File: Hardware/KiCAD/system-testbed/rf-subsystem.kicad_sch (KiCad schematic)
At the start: 86 parts, among them P1 SMA, P3 SMA, SW3 SKY13330-397LF, SW5 SKY13330-397LF, U3 CC1200RHBR, U4 TXS0101DBV, U6 LP5907MFX-2.5, X3 40 MHz

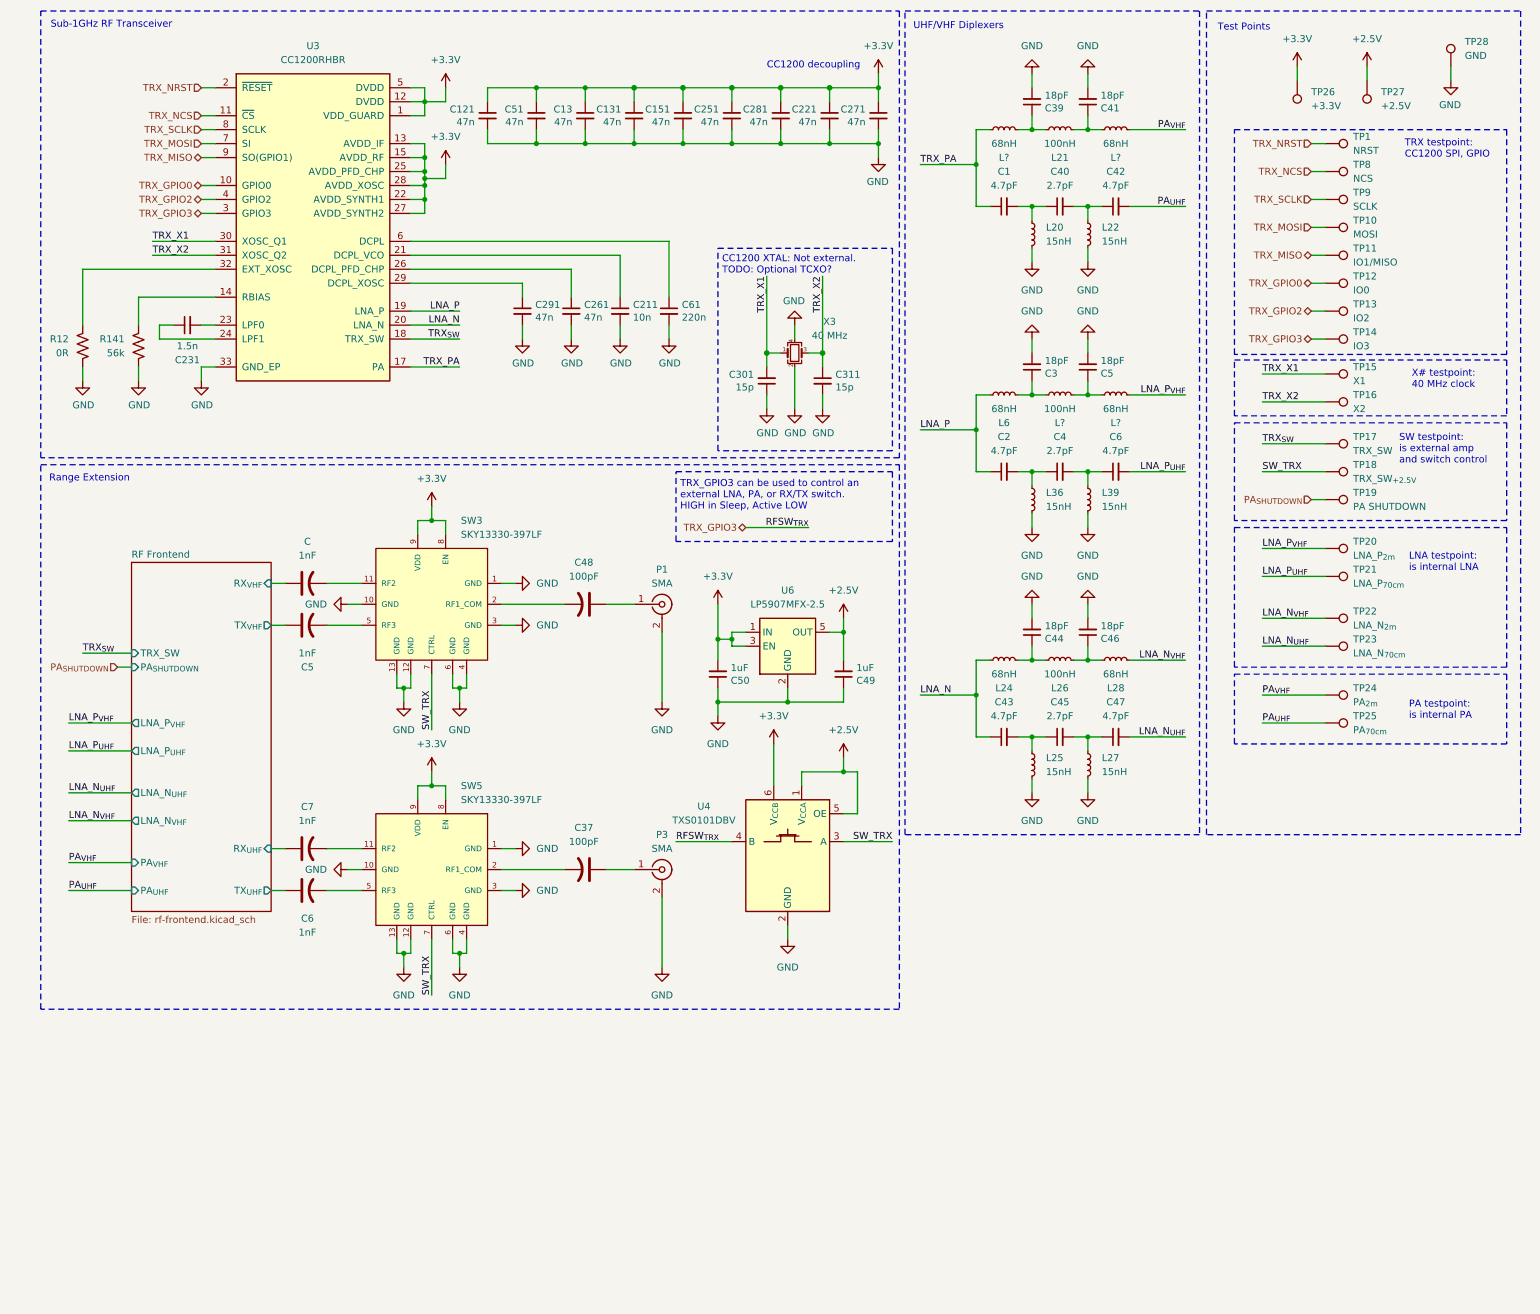
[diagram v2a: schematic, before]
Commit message: fix: reannotate schematics for pcb editor use #55
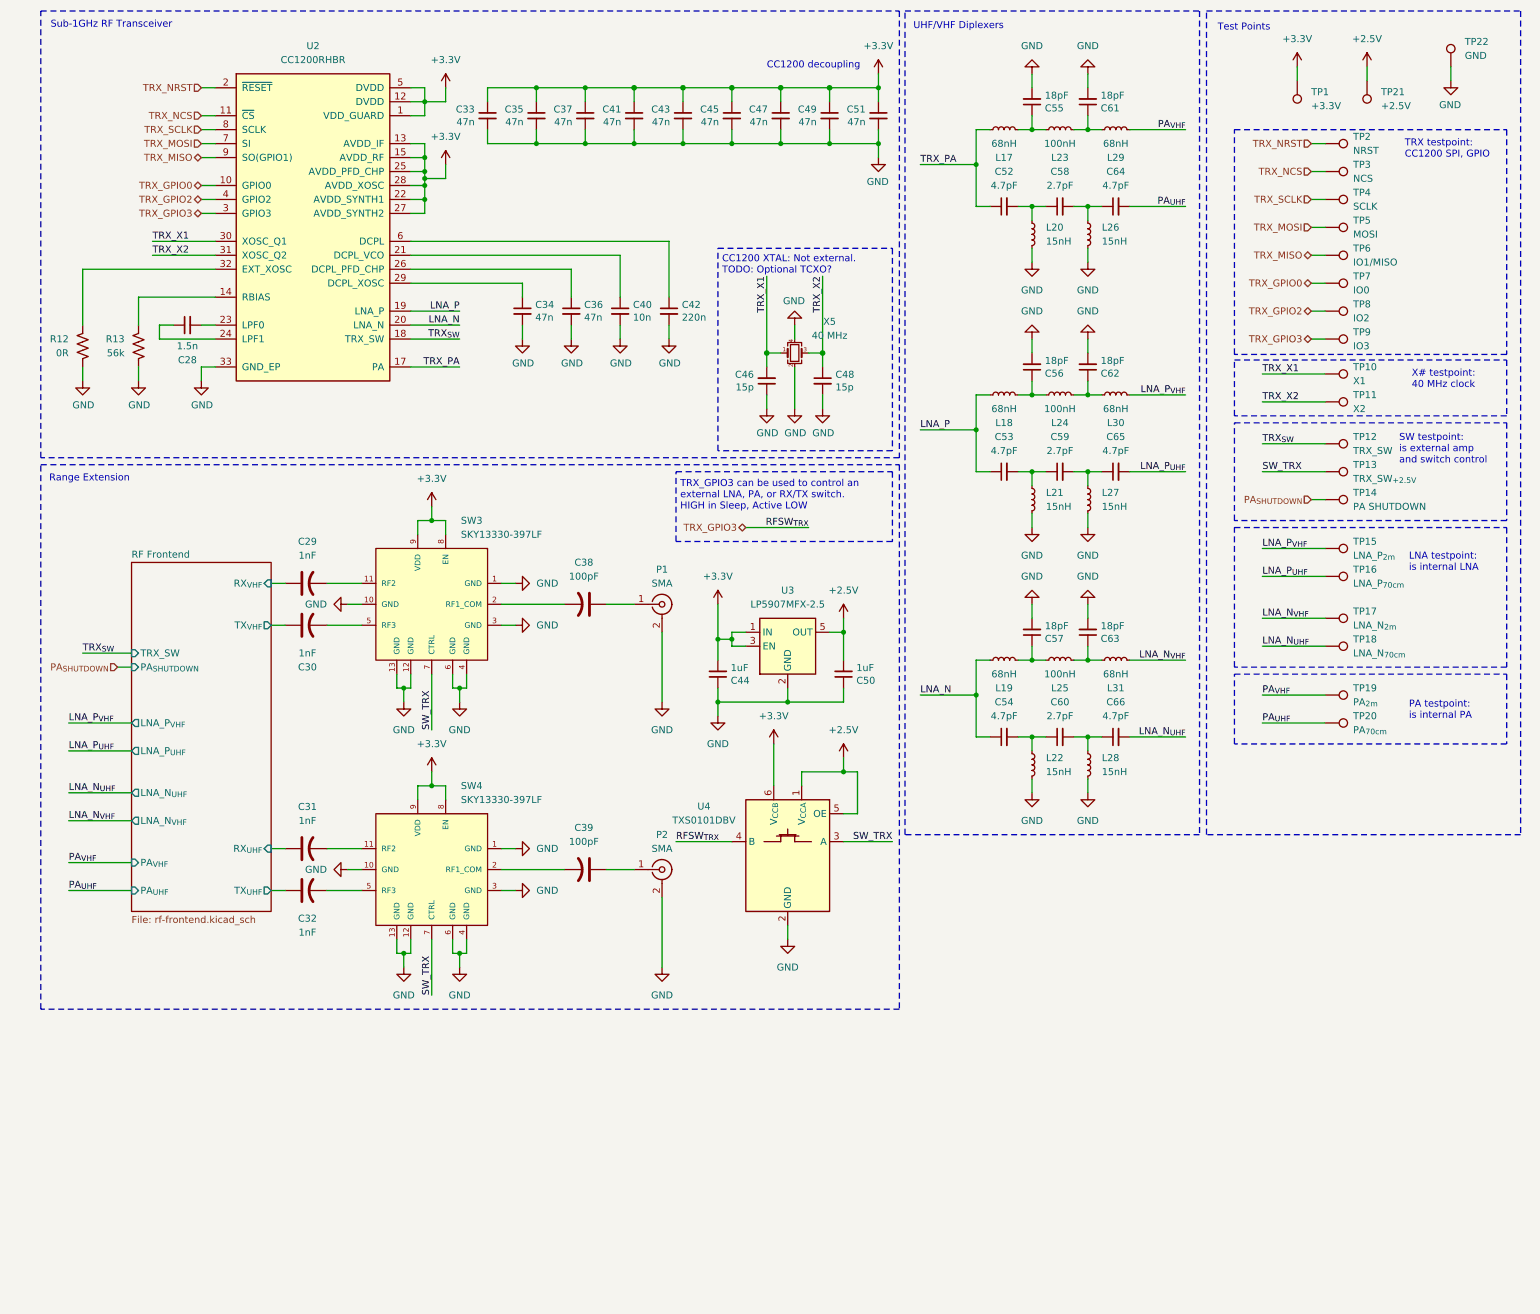
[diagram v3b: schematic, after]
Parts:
- C28: renamed from C231; footprint Capacitor_SMD:C_0603_1608Metric -> Capacitor_SMD:C_0402_1005Metric
- C29: renamed from C; footprint Capacitor_SMD:C_0603_1608Metric -> Capacitor_SMD:C_0402_1005Metric
- C30, C62: renamed from C5; footprint Capacitor_SMD:C_0603_1608Metric -> Capacitor_SMD:C_0402_1005Metric
- C31: renamed from C7; footprint Capacitor_SMD:C_0603_1608Metric -> Capacitor_SMD:C_0402_1005Metric
- C32: renamed from C6; footprint Capacitor_SMD:C_0603_1608Metric -> Capacitor_SMD:C_0402_1005Metric
- C33: renamed from C121; footprint Capacitor_SMD:C_0603_1608Metric -> Capacitor_SMD:C_0402_1005Metric
- C34: renamed from C291; footprint Capacitor_SMD:C_0603_1608Metric -> Capacitor_SMD:C_0402_1005Metric
- C35: renamed from C51; footprint Capacitor_SMD:C_0603_1608Metric -> Capacitor_SMD:C_0402_1005Metric
- C36: renamed from C261; footprint Capacitor_SMD:C_0603_1608Metric -> Capacitor_SMD:C_0402_1005Metric
- C37: renamed from C13; footprint Capacitor_SMD:C_0603_1608Metric -> Capacitor_SMD:C_0402_1005Metric
- C38: renamed from C48; footprint Capacitor_SMD:C_0603_1608Metric -> Capacitor_SMD:C_0402_1005Metric
- C39: renamed from C37; footprint Capacitor_SMD:C_0603_1608Metric -> Capacitor_SMD:C_0402_1005Metric
- C40: renamed from C211; footprint Capacitor_SMD:C_0603_1608Metric -> Capacitor_SMD:C_0402_1005Metric
- C41: renamed from C131; footprint Capacitor_SMD:C_0603_1608Metric -> Capacitor_SMD:C_0402_1005Metric
- C42: renamed from C61; footprint Capacitor_SMD:C_0603_1608Metric -> Capacitor_SMD:C_0402_1005Metric
- C43: renamed from C151; footprint Capacitor_SMD:C_0603_1608Metric -> Capacitor_SMD:C_0402_1005Metric
- C44: renamed from C50; footprint Capacitor_SMD:C_0603_1608Metric -> Capacitor_SMD:C_0402_1005Metric
- C45: renamed from C251; footprint Capacitor_SMD:C_0603_1608Metric -> Capacitor_SMD:C_0402_1005Metric
- C46: renamed from C301; footprint Capacitor_SMD:C_0603_1608Metric -> Capacitor_SMD:C_0402_1005Metric
- C47: renamed from C281; footprint Capacitor_SMD:C_0603_1608Metric -> Capacitor_SMD:C_0402_1005Metric
- C48: renamed from C311; footprint Capacitor_SMD:C_0603_1608Metric -> Capacitor_SMD:C_0402_1005Metric
- C49: renamed from C221; footprint Capacitor_SMD:C_0603_1608Metric -> Capacitor_SMD:C_0402_1005Metric
- C51: renamed from C271; footprint Capacitor_SMD:C_0603_1608Metric -> Capacitor_SMD:C_0402_1005Metric
- C52: renamed from C1; footprint (none) -> Capacitor_SMD:C_0402_1005Metric
- C53: renamed from C2; footprint (none) -> Capacitor_SMD:C_0402_1005Metric
- C54: renamed from C43; footprint (none) -> Capacitor_SMD:C_0402_1005Metric
- C55: renamed from C39; footprint Capacitor_SMD:C_0603_1608Metric -> Capacitor_SMD:C_0402_1005Metric
- C56: renamed from C3; footprint Capacitor_SMD:C_0603_1608Metric -> Capacitor_SMD:C_0402_1005Metric
- C57: renamed from C44; footprint Capacitor_SMD:C_0603_1608Metric -> Capacitor_SMD:C_0402_1005Metric
- C58: renamed from C40; footprint (none) -> Capacitor_SMD:C_0402_1005Metric
- C59: renamed from C4; footprint (none) -> Capacitor_SMD:C_0402_1005Metric
- C60: renamed from C45; footprint (none) -> Capacitor_SMD:C_0402_1005Metric
- C61: renamed from C41; footprint Capacitor_SMD:C_0603_1608Metric -> Capacitor_SMD:C_0402_1005Metric
- C63: renamed from C46; footprint Capacitor_SMD:C_0603_1608Metric -> Capacitor_SMD:C_0402_1005Metric
- C64: renamed from C42; footprint (none) -> Capacitor_SMD:C_0402_1005Metric
- C65: renamed from C6; footprint (none) -> Capacitor_SMD:C_0402_1005Metric
- C66: renamed from C47; footprint (none) -> Capacitor_SMD:C_0402_1005Metric
- L17, L24, L29, L30: renamed from L?; footprint (none) -> Inductor_SMD:L_0402_1005Metric
- L18: renamed from L6; footprint (none) -> Inductor_SMD:L_0402_1005Metric
- L19: renamed from L24; footprint (none) -> Inductor_SMD:L_0402_1005Metric
- L20: footprint Capacitor_SMD:C_0603_1608Metric -> Capacitor_SMD:C_0402_1005Metric
- L21: renamed from L36; footprint Capacitor_SMD:C_0603_1608Metric -> Capacitor_SMD:C_0402_1005Metric
- L22: renamed from L25; footprint Capacitor_SMD:C_0603_1608Metric -> Capacitor_SMD:C_0402_1005Metric
- L23: renamed from L21; footprint (none) -> Inductor_SMD:L_0402_1005Metric
- L25: renamed from L26; footprint (none) -> Inductor_SMD:L_0402_1005Metric
- L26: renamed from L22; footprint Capacitor_SMD:C_0603_1608Metric -> Capacitor_SMD:C_0402_1005Metric
- L27: renamed from L39; footprint Capacitor_SMD:C_0603_1608Metric -> Capacitor_SMD:C_0402_1005Metric
- L28: renamed from L27; footprint Capacitor_SMD:C_0603_1608Metric -> Capacitor_SMD:C_0402_1005Metric
- L31: renamed from L28; footprint (none) -> Inductor_SMD:L_0402_1005Metric
- P1: footprint Connector_Coaxial:SMA_Amphenol_901-143_Horizontal -> Connector_Coaxial:SMA_Amphenol_901-144_Vertical
- P2: renamed from P3; footprint Connector_Coaxial:SMA_Amphenol_901-143_Horizontal -> Connector_Coaxial:SMA_Amphenol_901-144_Vertical
- R12: footprint Resistor_SMD:R_0603_1608Metric -> Resistor_SMD:R_0402_1005Metric
- R13: renamed from R141; footprint Resistor_SMD:R_0603_1608Metric -> Resistor_SMD:R_0402_1005Metric
- SW3: footprint SKY13330-397LF:SKY13330-397LF -> capstone-project:SKY13330-397LF
- SW4: renamed from SW5; footprint SKY13330-397LF:SKY13330-397LF -> capstone-project:SKY13330-397LF
- renumbered C49 to C50, TP26 to TP1, TP15 to TP10, TP16 to TP11, TP17 to TP12, TP18 to TP13, TP19 to TP14, TP20 to TP15, TP21 to TP16, TP22 to TP17, TP23 to TP18, TP24 to TP19, TP1 to TP2, TP25 to TP20, TP27 to TP21, TP28 to TP22, TP8 to TP3, TP9 to TP4, TP10 to TP5, TP11 to TP6, TP12 to TP7, TP13 to TP8, TP14 to TP9, U3 to U2, U6 to U3, X3 to X5

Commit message: fix: allow for DRC use in PCB editor by successful reannotation
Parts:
- C50: footprint Capacitor_SMD:C_0603_1608Metric -> Capacitor_SMD:C_0402_1005Metric
- C54: footprint Capacitor_SMD:C_0402_1005Metric -> Capacitor_SMD:C_0603_1608Metric
- L20, L21, L22, L26, L27, L28: footprint Capacitor_SMD:C_0402_1005Metric -> Inductor_SMD:L_0402_1005Metric
- TP1, TP10, TP11, TP12, TP13, TP14, TP15, TP16, TP17, TP18, TP19, TP2, TP20, TP21, TP22, TP3, TP4, TP5, TP6, TP7, TP8, TP9: footprint (none) -> TestPoint:TestPoint_Pad_D1.0mm
